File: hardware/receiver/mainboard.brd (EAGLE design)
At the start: 47.3 x 38.6 mm, 19 parts, among them J2 POWER_JACKPTH, J3 AVR_SPI_PRG_6PTH, Q1 MOSFET-NCHANNELAO3404A, U1 ATMEGA328P_TQFP, U2 RFM69HCW

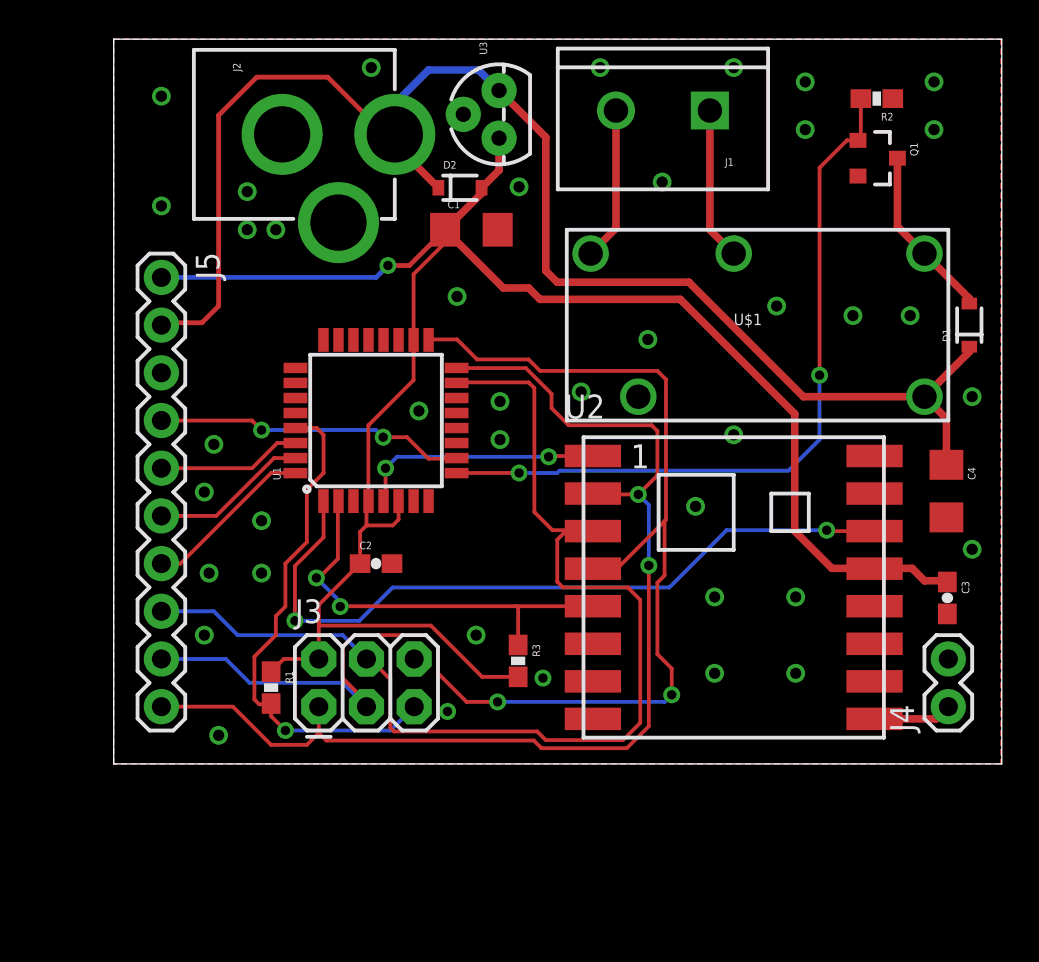
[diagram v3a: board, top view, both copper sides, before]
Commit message: Replaced relay and voltage regulator in schematic
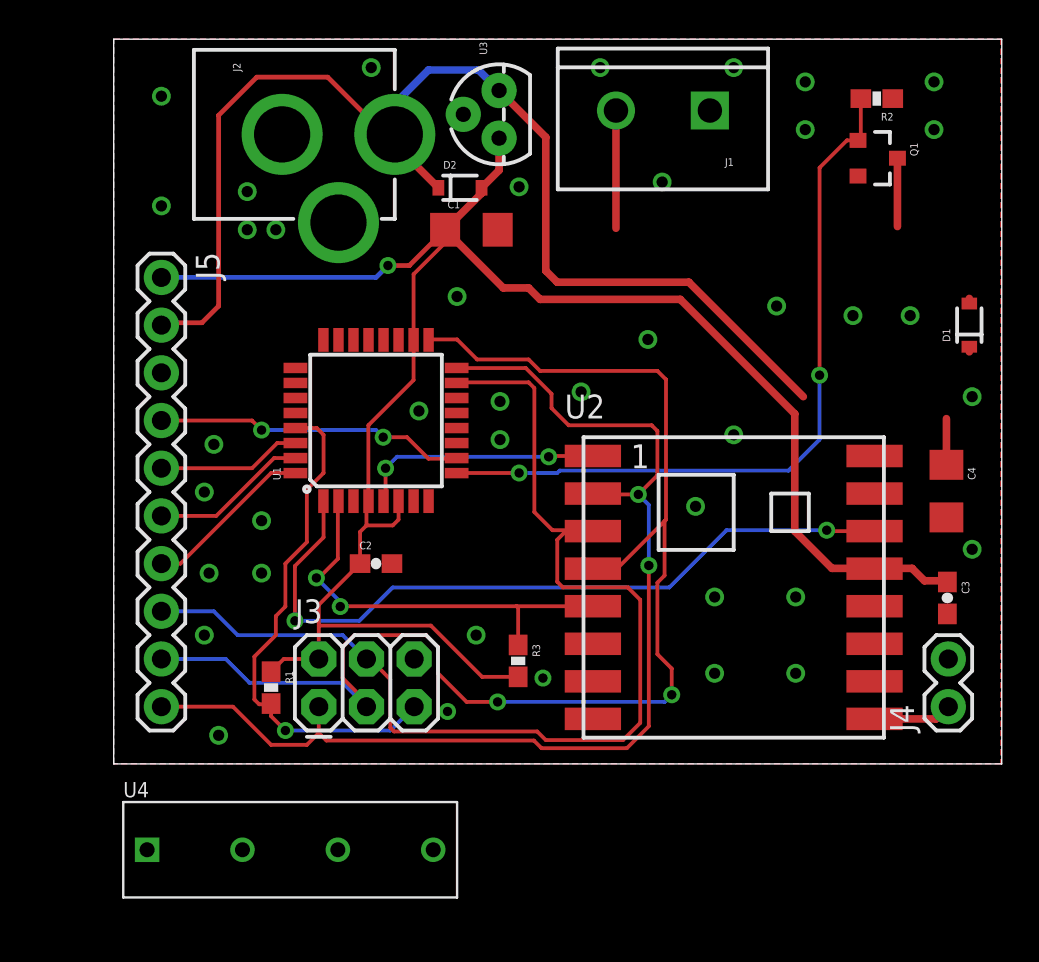
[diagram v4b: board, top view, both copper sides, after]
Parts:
- removed U$1: RELAYPTH, SparkFun-Electromechanical:RELAY-G5Q
- added U4: RELAY-9007, Electromechanical:RELAY-9007
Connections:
- net N$5: now also U4.1; no longer U$1.2
- net N$6: now also U4.4; no longer U$1.3
- net N$7: now also U4.3; no longer U$1.1
- net VIN: now also U4.2; no longer U$1.5
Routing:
- net VIN: track 78.9 -> 67.4 mm
- net N$5: track 8.15 -> 0.00 mm
- net N$7: track 9.33 -> 3.91 mm
- net N$6: track 8.18 -> 6.27 mm
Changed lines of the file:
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@@
 <element name="R1" library="SparkFun-Passives" package="0603-RES" value="10k" x="8.382" y="3.556" rot="R270"/>
 <element name="R2" library="SparkFun-Passives" package="0603-RES" value="10k" x="40.64" y="34.925" rot="R180"/>
-<element name="U$1" library="SparkFun-Electromechanical" package="RELAY-G5Q" value="RELAYPTH" x="34.29" y="22.86"/>
 <element name="U1" library="SparkFun-DigitalIC" package="TQFP32-08" value="ATMEGA328P_TQFP" x="13.97" y="17.78" rot="R90">
 <attribute name="PROD_ID" value="IC-09069" x="13.97" y="17.78" size="1.778" layer="27" rot="R90" display="off"/>
@@
 <attribute name="PROD_ID" value="DIO-09646" x="18.4404" y="30.1752" size="1.778" layer="27" display="off"/>
 </element>
+<element name="U4" library="Electromechanical" package="RELAY-9007" value="RELAY-9007" x="9.398" y="-5.08"/>
 </elements>
 <signals>
@@
 <wire x1="43.8" y1="1.89" x2="44.45" y2="2.54" width="0.4064" layer="1"/>
 </signal>
-<signal name="N$5">
-<contactref element="U$1" pad="2"/>
-<contactref element="J1" pad="1"/>
-<wire x1="31.75" y1="34.29" x2="31.75" y2="27.94" width="0.4064" layer="1"/>
-<wire x1="31.75" y1="27.94" x2="33.02" y2="26.67" width="0.4064" layer="1"/>
-</signal>
 <signal name="N$6">
 <contactref element="J1" pad="2"/>
-<contactref element="U$1" pad="3"/>
 <wire x1="26.75" y1="34.29" x2="26.75" y2="28.02" width="0.4064" layer="1"/>
-<wire x1="26.75" y1="28.02" x2="25.4" y2="26.67" width="0.4064" layer="1"/>
+<contactref element="U4" pad="4"/>
+<wire x1="17.018" y1="-5.08" x2="26.75" y2="28.02" width="0" layer="19" extent="1-1"/>
 </signal>
 <signal name="N$7">
 <contactref element="Q1" pad="3"/>
-<contactref element="U$1" pad="1"/>
 <wire x1="41.74" y1="31.75" x2="41.74" y2="28.11" width="0.4064" layer="1"/>
-<wire x1="41.74" y1="28.11" x2="43.18" y2="26.67" width="0.4064" layer="1"/>
 <contactref element="D1" pad="A"/>
 <wire x1="45.5676" y1="24.01" x2="45.5676" y2="24.2824" width="0.4064" layer="1"/>
-<wire x1="45.5676" y1="24.2824" x2="43.18" y2="26.67" width="0.4064" layer="1"/>
+<contactref element="U4" pad="3"/>
+<wire x1="45.5676" y1="24.2824" x2="41.74" y2="28.11" width="0" layer="19" extent="1-1"/>
+<wire x1="11.938" y1="-5.08" x2="45.5676" y2="24.01" width="0" layer="19" extent="1-1"/>
 </signal>
 <signal name="N$8">
@@
 <contactref element="J2" pad="PWR"/>
 <contactref element="U3" pad="3"/>
-<contactref element="U$1" pad="5"/>
 <contactref element="D1" pad="C"/>
 <contactref element="C4" pad="1"/>
 <wire x1="45.5676" y1="21.71" x2="45.5676" y2="21.4376" width="0.4064" layer="1"/>
-<wire x1="45.5676" y1="21.4376" x2="43.18" y2="19.05" width="0.4064" layer="1"/>
 <wire x1="44.3484" y1="15.4208" x2="44.3484" y2="17.8816" width="0.4064" layer="1"/>
-<wire x1="44.3484" y1="17.8816" x2="43.18" y2="19.05" width="0.4064" layer="1"/>
 <contactref element="D2" pad="C"/>
 <contactref element="J5" pad="2"/>
 <wire x1="14.97" y1="32.4956" x2="17.2904" y2="30.1752" width="0.4064" layer="1"/>
-<wire x1="43.18" y1="19.05" x2="36.7284" y2="19.05" width="0.4064" layer="1"/>
 <wire x1="30.6324" y1="25.146" x2="23.622" y2="25.146" width="0.4064" layer="1"/>
 <wire x1="23.622" y1="25.146" x2="23.0124" y2="25.7556" width="0.4064" layer="1"/>
@@
 <wire x1="19.431" y1="36.449" x2="20.5232" y2="35.3568" width="0.4064" layer="16"/>
 <wire x1="14.97" y1="32.4956" x2="14.97" y2="33.02" width="0.4064" layer="1"/>
+<contactref element="U4" pad="2"/>
+<wire x1="44.3484" y1="17.8816" x2="45.5676" y2="21.4376" width="0" layer="19" extent="1-1"/>
+<wire x1="36.7284" y1="19.05" x2="44.3484" y2="17.8816" width="0" layer="19" extent="1-1"/>
+<wire x1="6.858" y1="-5.08" x2="4.699" y2="22.987" width="0" layer="19" extent="1-1"/>
 </signal>
 <signal name="N$9">
@@
 <wire x1="7.366" y1="15.24" x2="2.54" y2="15.24" width="0.2032" layer="1"/>
 </signal>
+<signal name="N$5">
+<contactref element="U4" pad="1"/>
+<contactref element="J1" pad="1"/>
+<wire x1="1.778" y1="-5.08" x2="31.75" y2="34.29" width="0" layer="19" extent="1-1"/>
+</signal>
 </signals>

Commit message: Replaced LDO and relay and  updated BOM
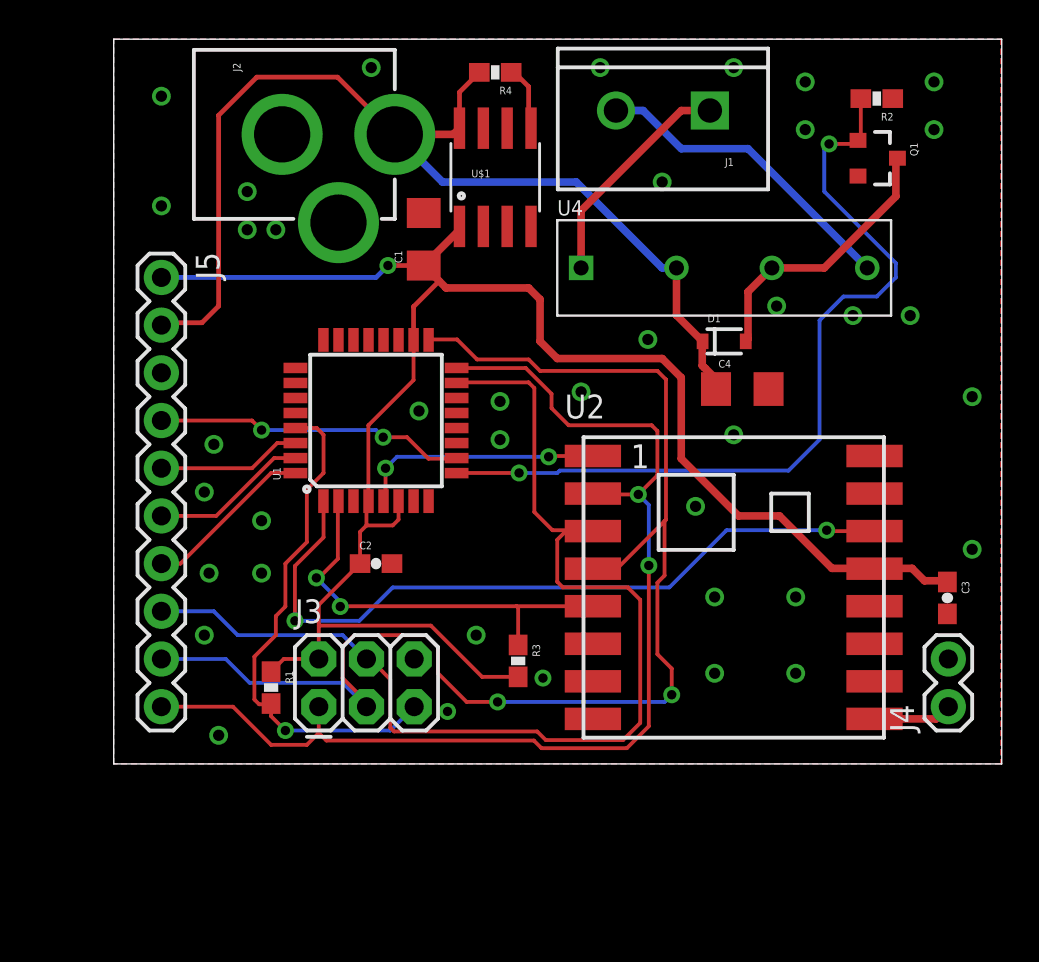
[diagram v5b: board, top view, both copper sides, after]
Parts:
- removed D2: (no value), SparkFun-DiscreteSemi:SOD-323
- removed U3: (no value), SparkFun-PowerIC:TO-92
- added R4: 51k, SparkFun-Passives:0603-RES
- added U$1: LM2931, SparkFun-PowerIC:SO08
- moved U4 38.7 mm to (32.5, 25.9)
- moved D1 13.1 mm to (32.5, 22.0), turned to 0 degrees
- moved C4 12.2 mm to (33.5, 19.5), turned to 0 degrees
- moved C1 2.59 mm to (16.5, 27.4), turned to 90 degrees
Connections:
- new net N$19: R4.1, U$1.5
- net GND: now also U$1.2, U$1.3, U$1.6, U$1.7; no longer U3.2
- net VCC: now also U$1.1; no longer D2.A, U3.1
- net VIN: now also R4.2, U$1.8; no longer D2.C, U3.3
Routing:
- net N$5: track 0.00 -> 12.1 mm
- net N$7: track 3.91 -> 14.7 mm
- net N$6: track 6.27 -> 16.9 mm
- net VIN: track 67.4 -> 57.4 mm
- net VCC: track 103.3 -> 96.1 mm
- net N$8: track 39.5 -> 44.1 mm
- net N$19: track 0.00 -> 3.51 mm
- net GND: vias 43 -> 41

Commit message: Added ground plane vias
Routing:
- net GND: vias 41 -> 43
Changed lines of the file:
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@@
 <contactref element="U$1" pad="3"/>
 <contactref element="C1" pad="2"/>
+<via x="17.018" y="36.068" extent="1-16" drill="0.6"/>
+<via x="20.32" y="31.496" extent="1-16" drill="0.6"/>
 </signal>
 <signal name="VCC">

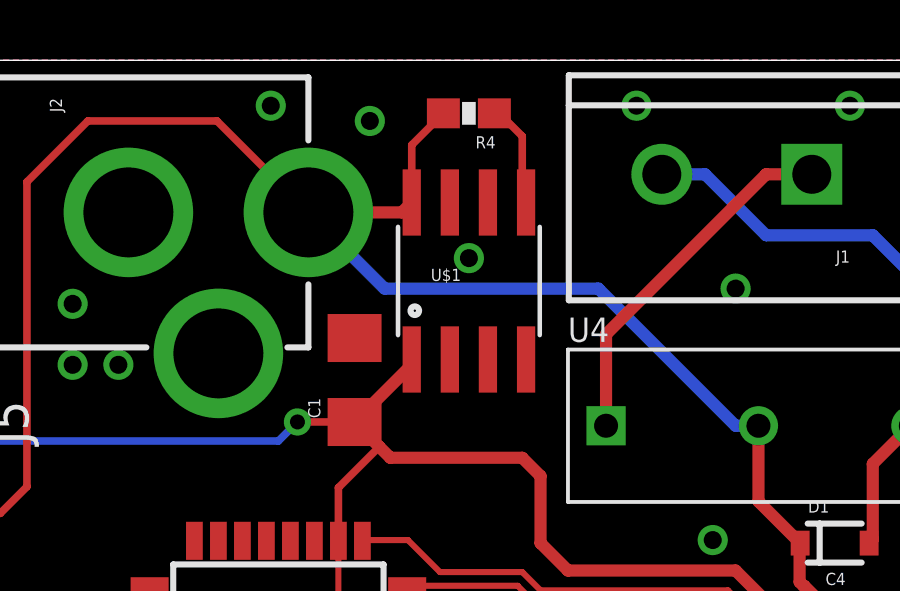
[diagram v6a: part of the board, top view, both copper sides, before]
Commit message: Added frames
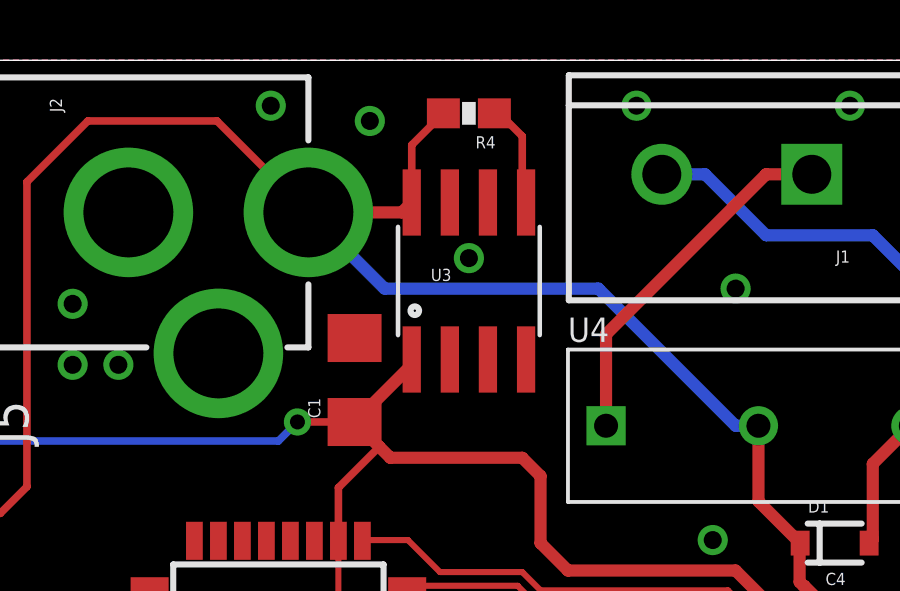
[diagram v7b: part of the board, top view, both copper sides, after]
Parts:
- renumbered U$1 to U3
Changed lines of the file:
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@@
 <element name="R3" library="SparkFun-Passives" package="0603-RES" value="47k" x="21.5392" y="4.9784" rot="R270"/>
 <element name="U4" library="Electromechanical" package="RELAY-9007" value="RELAY-9007" x="32.512" y="25.908"/>
-<element name="U$1" library="SparkFun-PowerIC" package="SO08" value="LM2931" x="20.32" y="30.734"/>
+<element name="U3" library="SparkFun-PowerIC" package="SO08" value="LM2931" x="20.32" y="30.734"/>
 <element name="R4" library="SparkFun-Passives" package="0603-RES" value="51k" x="20.32" y="36.322" rot="R180"/>
 </elements>
@@
 <contactref element="J2" pad="GNDBREAK"/>
 <contactref element="J2" pad="GND"/>
-<contactref element="U$1" pad="6"/>
-<contactref element="U$1" pad="7"/>
-<contactref element="U$1" pad="2"/>
-<contactref element="U$1" pad="3"/>
+<contactref element="U3" pad="6"/>
+<contactref element="U3" pad="7"/>
+<contactref element="U3" pad="2"/>
+<contactref element="U3" pad="3"/>
 <contactref element="C1" pad="2"/>
 <via x="17.018" y="36.068" extent="1-16" drill="0.6"/>
@@
 <wire x1="15.17" y1="12.503" x2="14.859" y2="12.192" width="0.2032" layer="1"/>
 <wire x1="14.859" y1="12.192" x2="13.462" y2="12.192" width="0.2032" layer="1"/>
-<contactref element="U$1" pad="1"/>
+<contactref element="U3" pad="1"/>
 <contactref element="C1" pad="1"/>
 <wire x1="14.605" y1="26.035" x2="16.507" y2="26.035" width="0.254" layer="1"/>
@@
 <contactref element="U4" pad="2"/>
 <contactref element="J2" pad="PWR"/>
-<contactref element="U$1" pad="8"/>
+<contactref element="U3" pad="8"/>
 <contactref element="R4" pad="2"/>
 <wire x1="14.97" y1="33.02" x2="18.0848" y2="33.02" width="0.4064" layer="1"/>
@@
 <signal name="N$19">
 <contactref element="R4" pad="1"/>
-<contactref element="U$1" pad="5"/>
+<contactref element="U3" pad="5"/>
 <wire x1="21.17" y1="36.322" x2="21.336" y2="36.322" width="0.254" layer="1"/>
 <wire x1="21.336" y1="36.322" x2="22.098" y2="35.56" width="0.254" layer="1"/>
